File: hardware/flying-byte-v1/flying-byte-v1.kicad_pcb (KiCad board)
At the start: 4 copper layers, 52 x 25 mm, 51 parts, among them J1 Conn_Coaxial, J2 Conn_ARM_SWD_TagConnect_TC2030, J3 USB_C_Receptacle_USB2.0, J4 Conn_01x04, SW1 SW_Push, U1 STM32WB55CEU6, U2 USBLC6-2SC6_MOD, U3 MIC5365-3.3YD5, X1 32MHz, X2 32kHz768

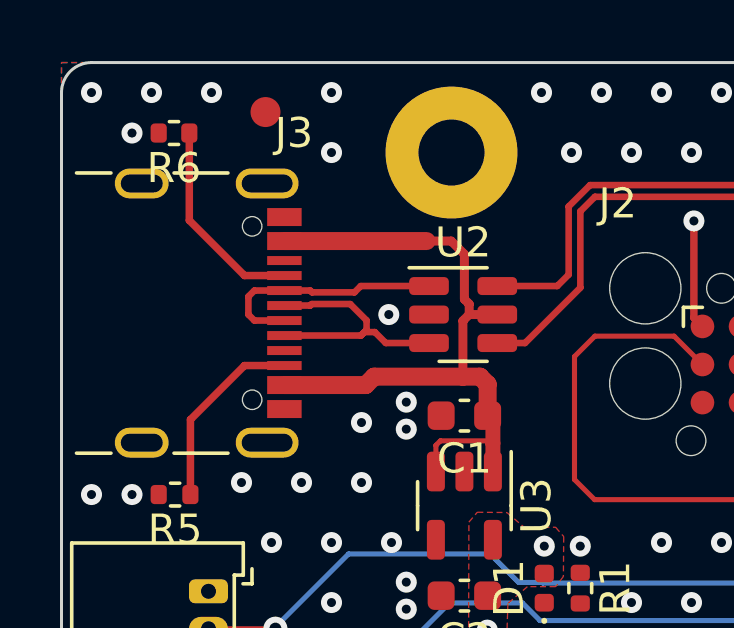
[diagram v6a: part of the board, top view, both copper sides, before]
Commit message: fix: Resolve DRC errors #1
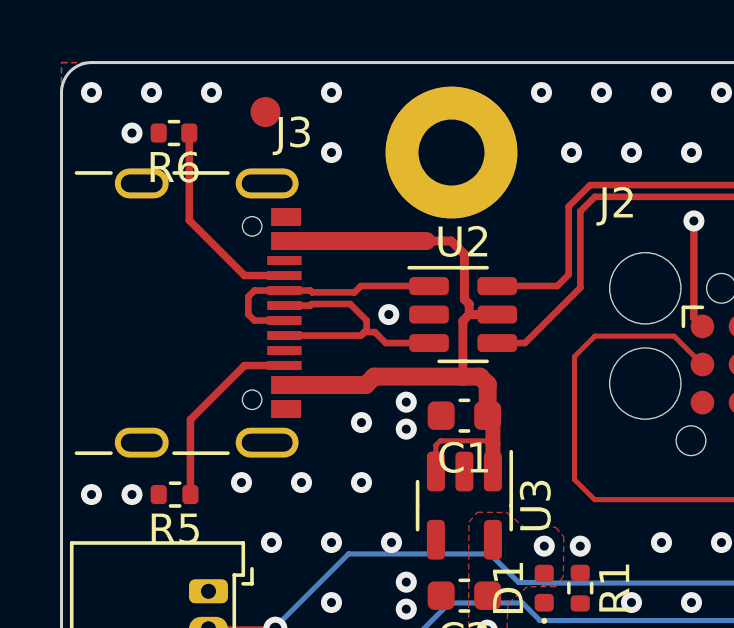
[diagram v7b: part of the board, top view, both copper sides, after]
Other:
- rule pad_to_mask_clearance: 0.08 -> 0

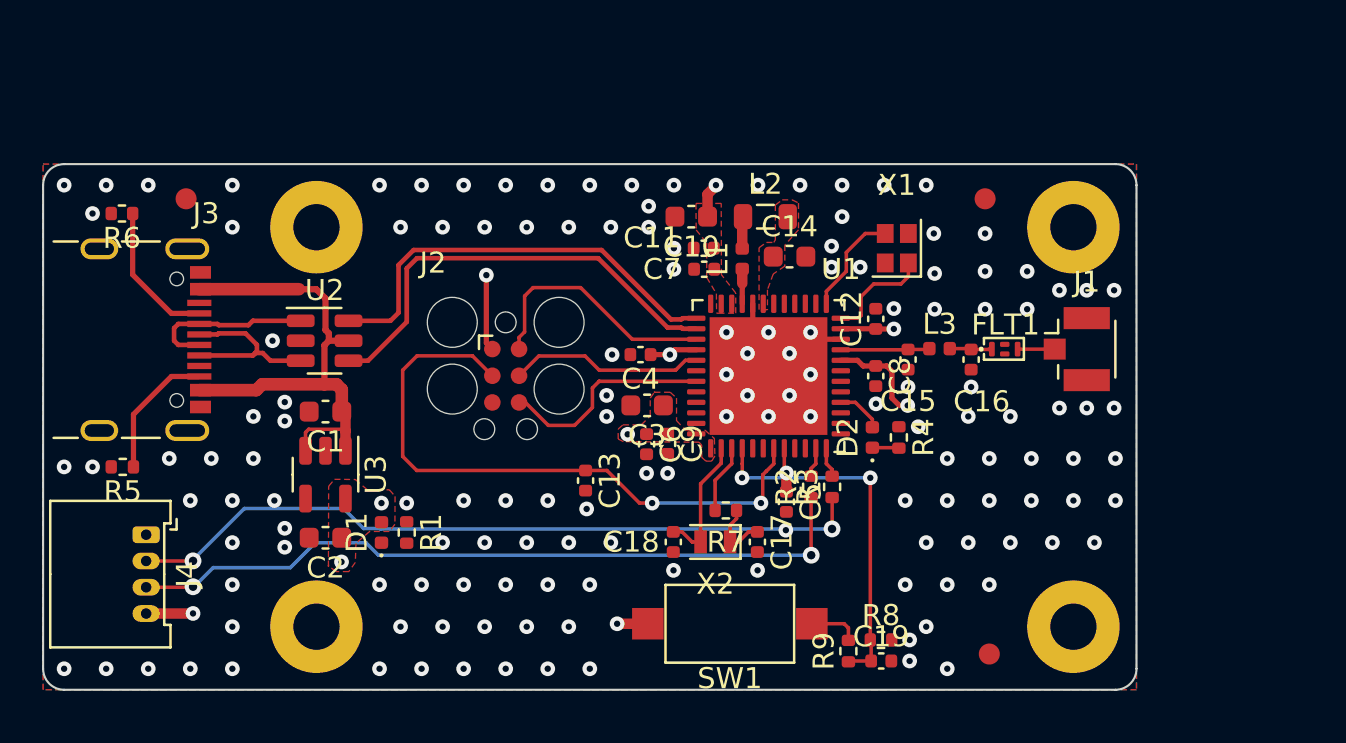
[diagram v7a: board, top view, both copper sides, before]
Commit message: fix: Resolve DRC errors #2
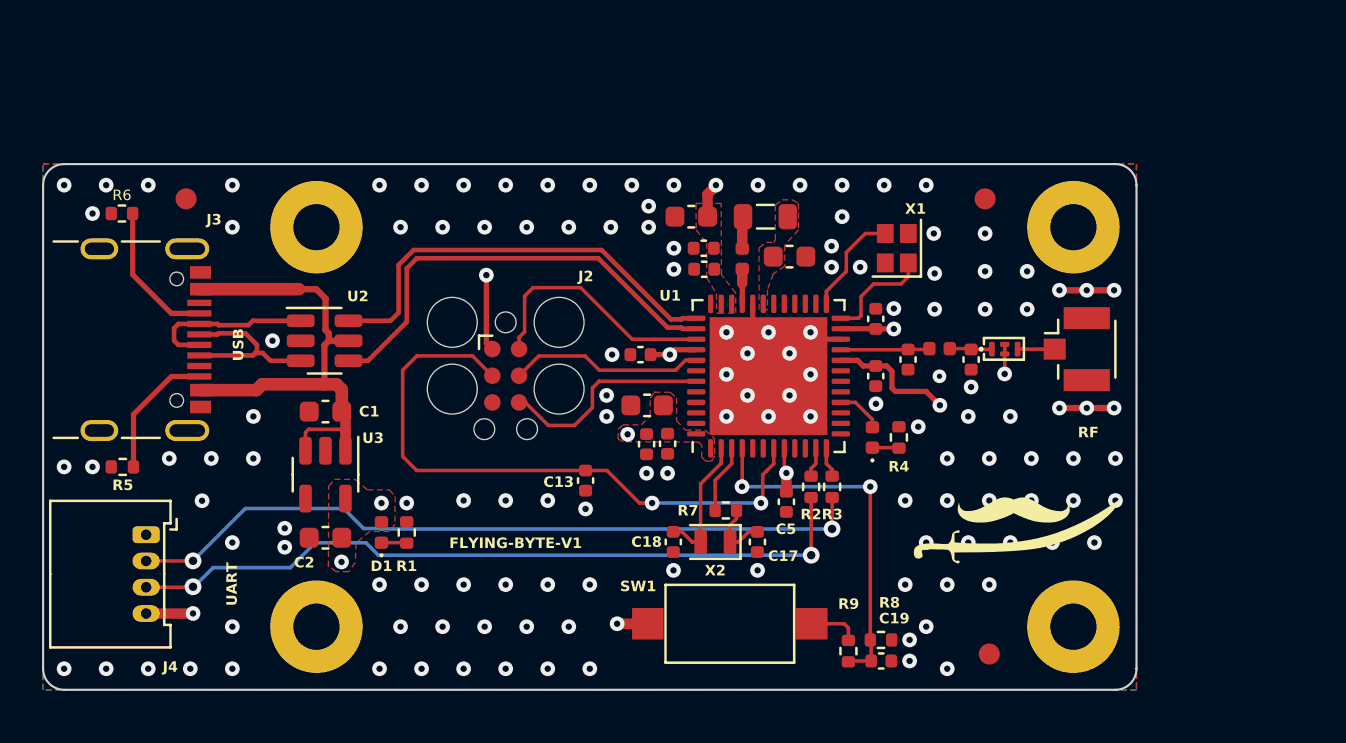
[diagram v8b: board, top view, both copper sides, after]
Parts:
- added G***: LOGO, icons:sabre-with-moustache, F.Cu at (139.3, 96.1)
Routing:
- net GND: track 7.91 -> 14.5 mm, vias 146 -> 136
- net +3V3: track 20.9 -> 22.1 mm
- net Net-(D1-K): track 0.00 -> 1.21 mm
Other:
- board text added: "FLYING-BYTE-V1"
- board text added: "RF"
- board text added: "UART"
- board text added: "USB"
